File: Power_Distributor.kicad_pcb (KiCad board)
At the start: 2 copper layers, 200 x 100 mm, 131 parts, among them J1 Thruster_Off_Switch, P1 XT60, P10 XT60, P15 XT60, P16 XT60, P17 XT60, P18 XT60, P19 USB_B, P2 XT60, P20 XT60, P21 XT60, P22 XT60, P23 XT60, P24 XT60, P25 XT60, P26 XT60, P27 XT60, P28 XT60, P29 XT60, P3 XT60, P4 XT60, P5 XT60, P6 XT60, P7 XT60, P8 XT60, P9 XT60, Q1 IPD90P03P4L, Q2 IPD90P03P4L, Q3 IPD90P03P4L, Q4 IPD90P03P4L, Q6 IPD90P03P4L, Q7 AUIRFS8409-7P, Q8 AUIRFS8409-7P, Q9 BC817-40, U1 93LC56BT-I/OT, U10 I6A24014A033V, U2 FT232H, U3 ACPL-247-500E, U4 ACPL-247-500E, U5 LTC4357, U6 LTC4357, U7 UWE-12/6-Q12P, U8 TEN_20-2411WIN, U9 TEN_20-2411WIN, Y1 12MHz

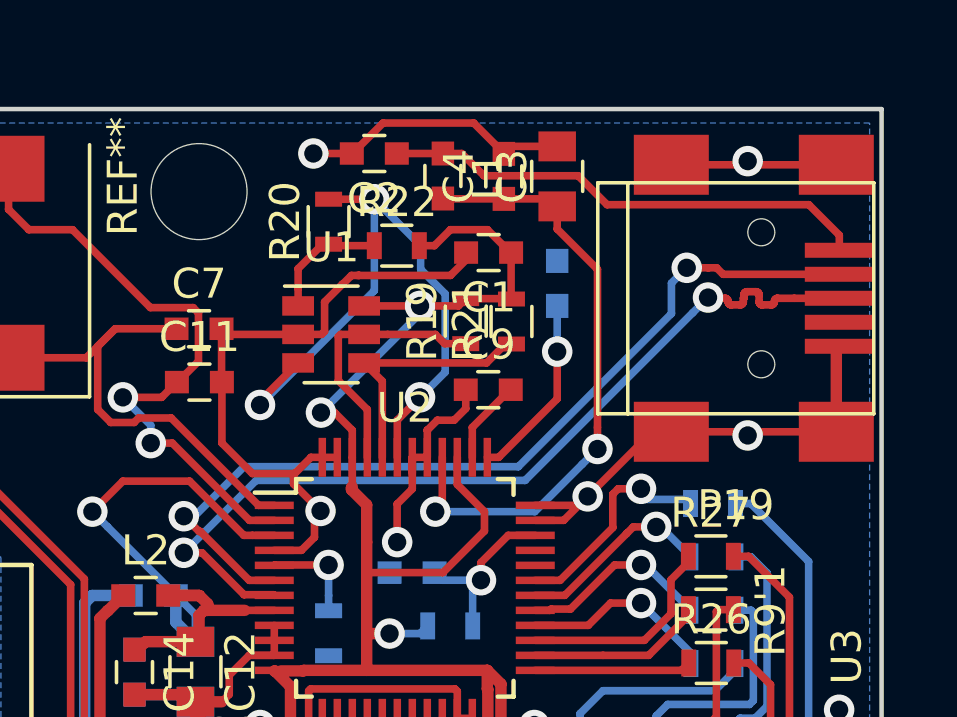
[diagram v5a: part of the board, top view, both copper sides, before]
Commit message: fix USB connector and fill GNDD zone
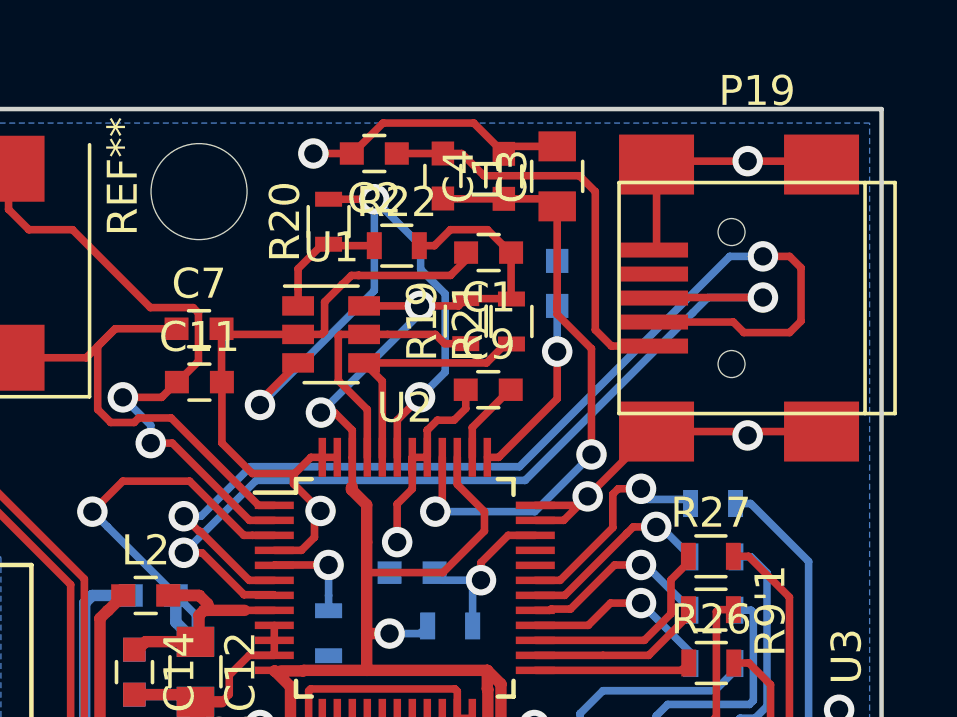
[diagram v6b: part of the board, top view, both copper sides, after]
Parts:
- moved P19 0.59 mm to (240.2, 51.3), turned to 180 degrees
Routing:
- net /Power_Controller/D-: track 29.9 -> 35.2 mm
- net Net-(C2-Pad1): track 16.4 -> 13.9 mm

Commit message: Another bug fixed
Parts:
- moved C10 3.67 mm to (234.2, 54.5)
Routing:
- net /Power_Controller/D-: track 35.2 -> 24.8 mm
- net Net-(C2-Pad1): track 13.9 -> 20.4 mm
- net /Power_Controller/D+: track 30.1 -> 24.8 mm
- net Net-(C10-Pad2): track 6.33 -> 3.28 mm
- net GNDD: track 109.6 -> 109.5 mm, vias 12 -> 13

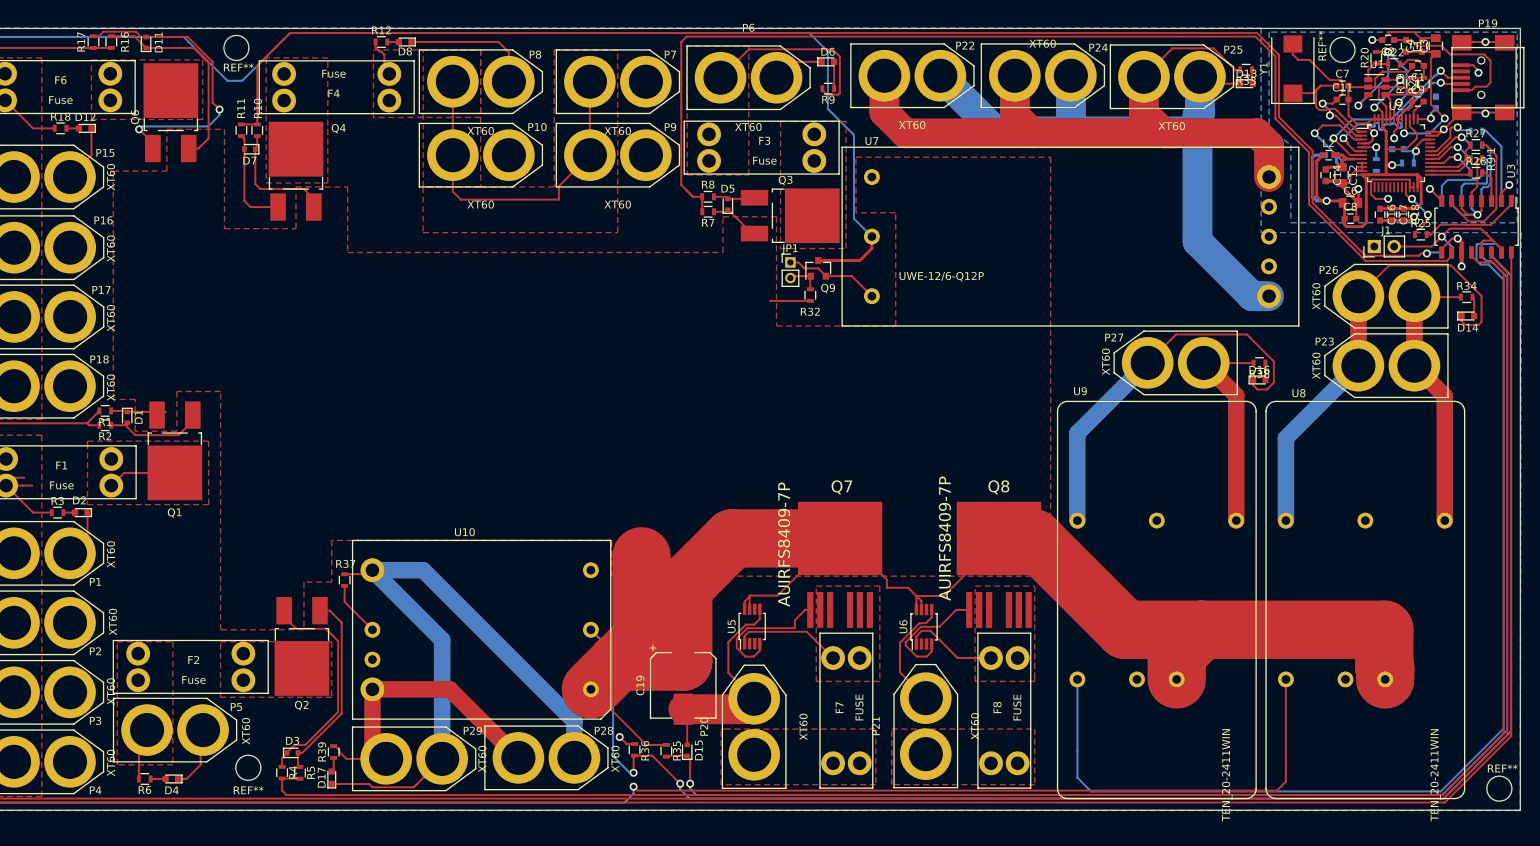
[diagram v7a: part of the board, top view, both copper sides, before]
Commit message: change circuit for i6a negative logic on/off
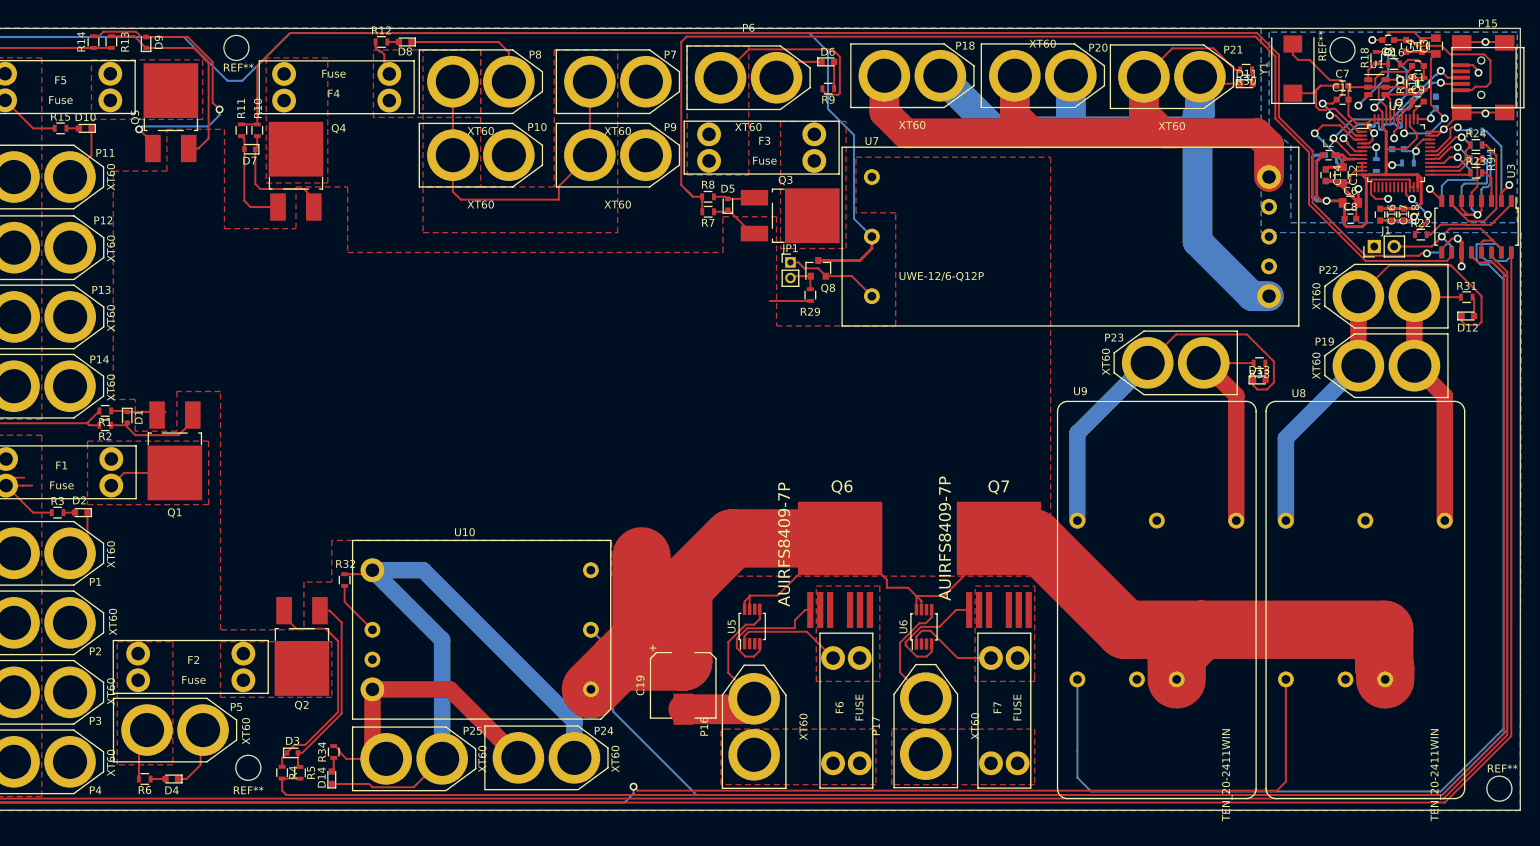
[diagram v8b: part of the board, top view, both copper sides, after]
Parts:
- removed D15: BZX585-C12, Diodes_SMD:D_SOD-523
- removed R35, R36: 10k, Resistors_SMD:R_0603
- R11, R2, R5, R8: value 1k -> 2.2k
- R14: renamed from R17; value 1k -> 2.2k
- R32: renamed from R37; value 1.4k -> 1k
- R34: renamed from R39; value 1k -> 2.2k
- renumbered D12 to D10, D13 to D11, D14 to D12, D16 to D13, D17 to D14, D11 to D9, F6 to F5, F7 to F6, F8 to F7, P15 to P11, P16 to P12, P17 to P13, P18 to P14, P19 to P15, P20 to P16, P21 to P17, P22 to P18, P23 to P19, P24 to P20, P25 to P21, P26 to P22, P27 to P23, P28 to P24, P29 to P25, Q6 to Q5, Q7 to Q6, Q8 to Q7, Q9 to Q8, R16 to R13, R18 to R15, R22 to R16, R19 to R17, R20 to R18, R21 to R19, R23 to R20, R24 to R21, R25 to R22, R26 to R23, R27 to R24, R28 to R25, R29 to R26, R30 to R27, R31 to R28, R32 to R29, R33 to R30, R34 to R31, R38 to R33
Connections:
- U10 pad 2: /DC-DC Converter/Lamp_SW_E -> /DC-DC Converter/Lamp_SW_C
- U4 pad 11: /DC-DC Converter/Lamp_SW_E -> GND
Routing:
- net /DC-DC Converter/Lamp_SW_E: track 204.2 -> 0.00 mm, vias 2 -> 0
- net /DC-DC Converter/Lamp_SW_C: track 178.1 -> 196.7 mm, vias 1 -> 0
- net +BATT: track 281.3 -> 268.7 mm
- net GND: track 115.1 -> 113.6 mm, vias 3 -> 2
